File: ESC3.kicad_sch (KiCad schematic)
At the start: 35 parts, among them J10 MOTOR_A, J11 MOTOR_B, J12 MOTOR_C, Q14 Q_NMOS_GDS, Q15 Q_NMOS_GDS, Q16 Q_NMOS_GDS, Q17 Q_NMOS_GDS, Q18 Q_NMOS_GDS, Q19 Q_NMOS_GDS, U18 STM32G071GBUxN, U19 DRV8300D

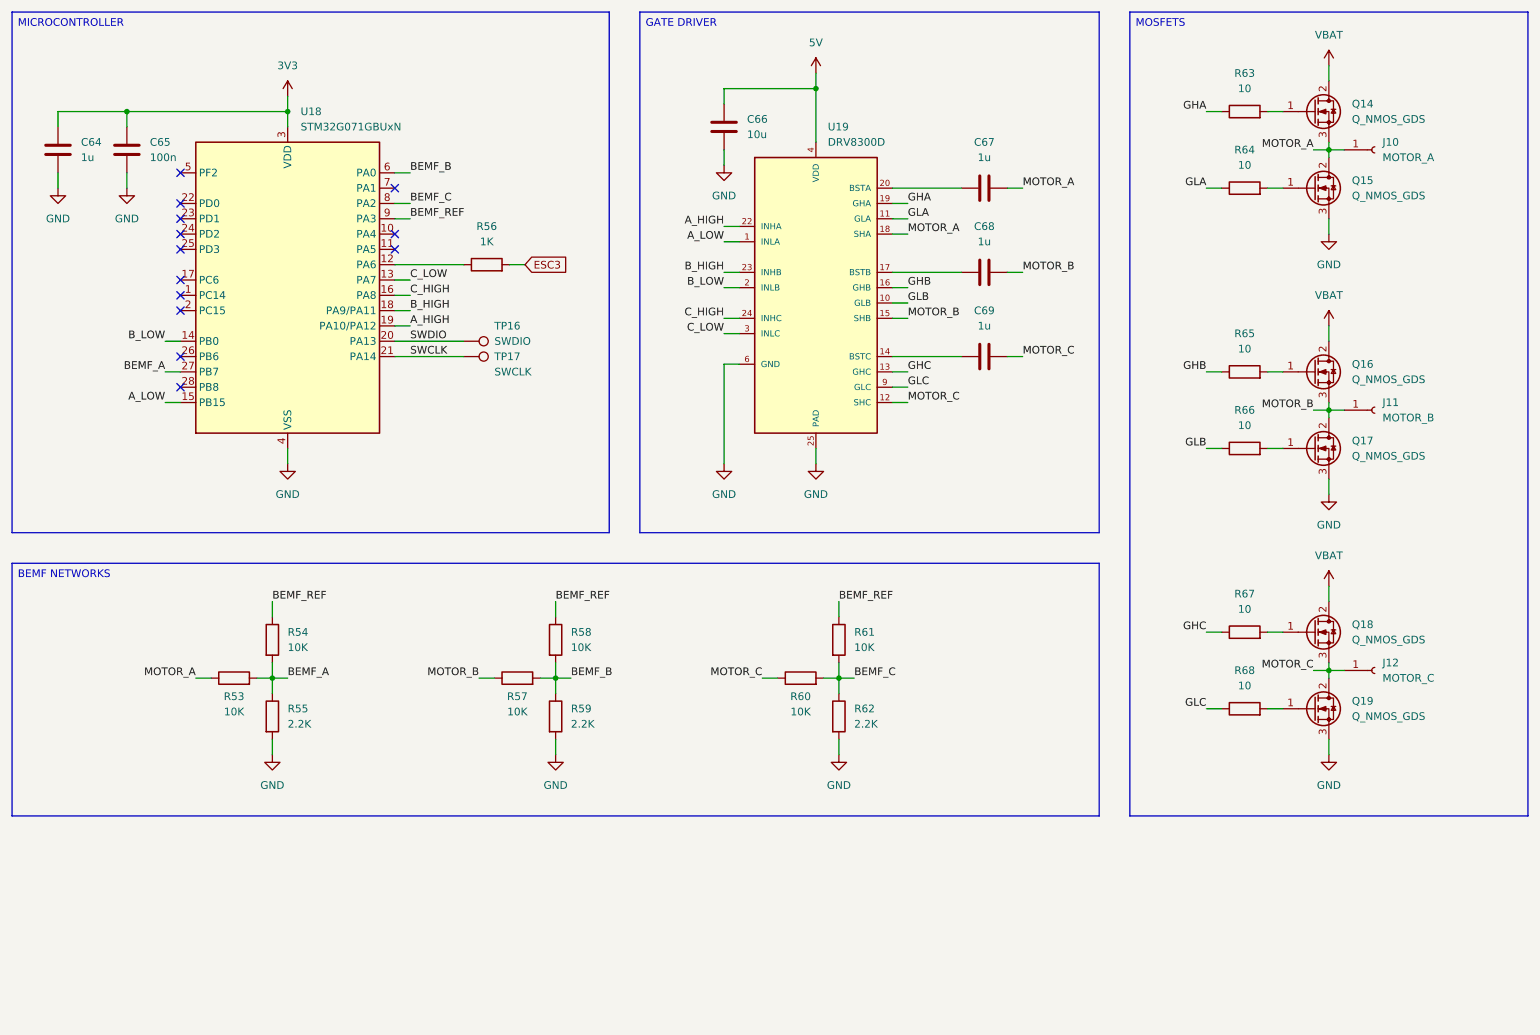
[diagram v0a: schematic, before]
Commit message: Footprints and revision
Added the missing footprints.
Updated a all the schematics.
Completed an initial review of the schematics.

TODO:
Perform a deep review of the schematics before committing to layout.
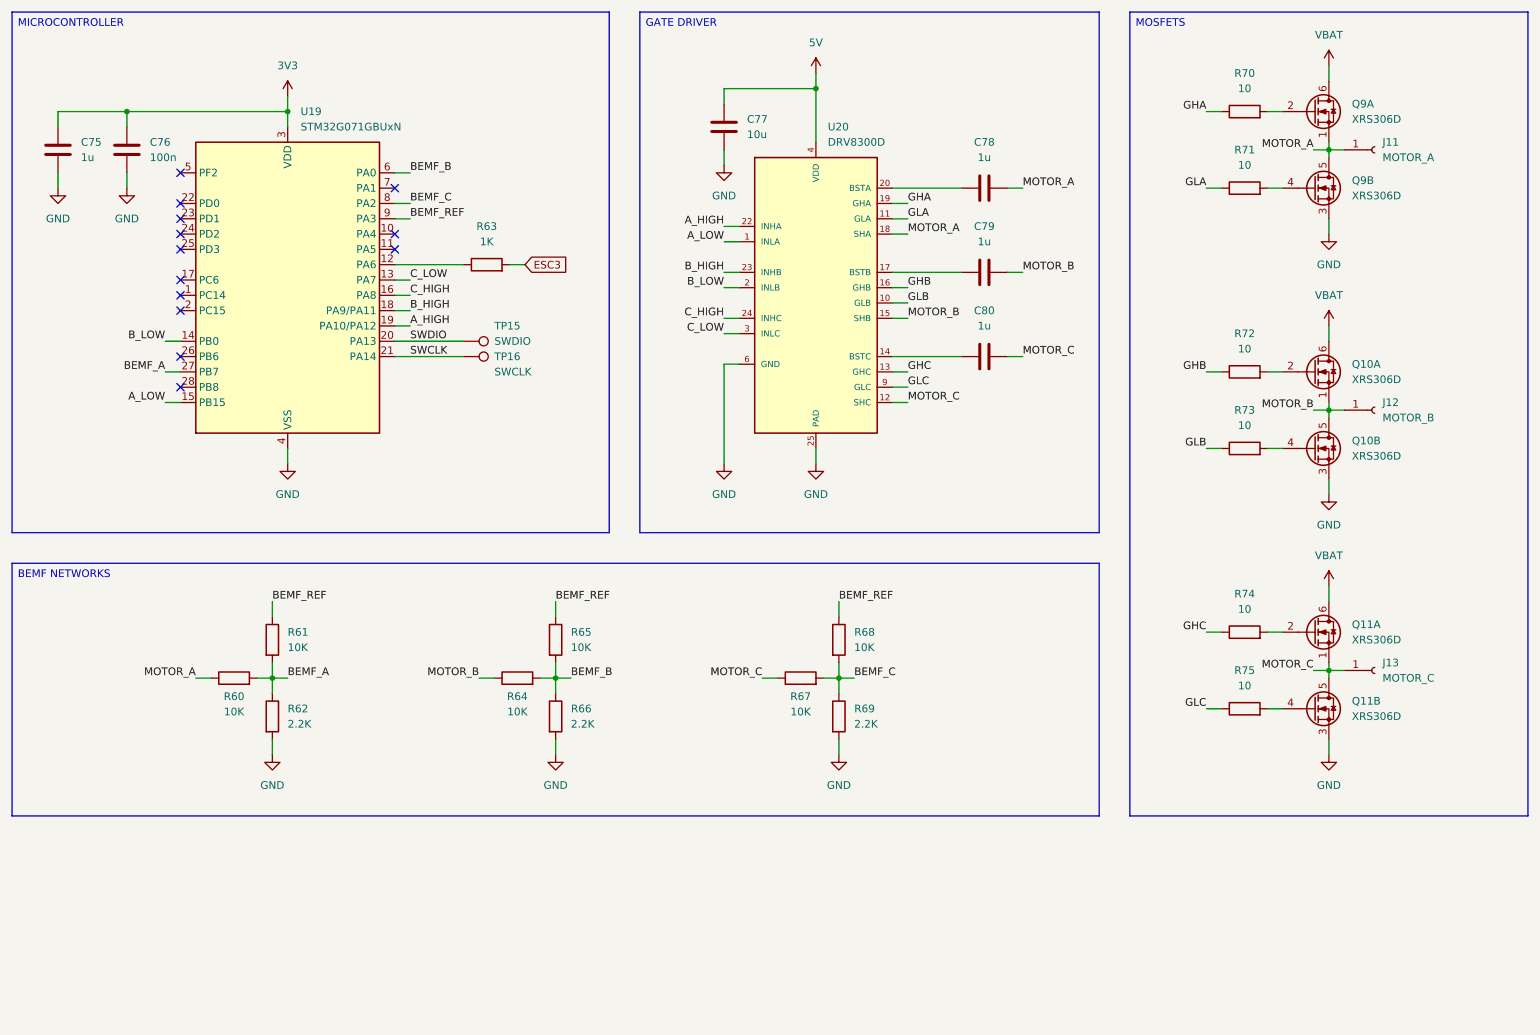
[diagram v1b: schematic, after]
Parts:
- removed Q14, Q15, Q16, Q17, Q18, Q19: Q_NMOS_GDS, symbol Transistor_FET:Q_NMOS_GDS
- added Q10, Q11, Q9: XRS306D, Custom_Parts:PDFN8, symbol Transistor_FET:Q_Dual_NMOS_S1G1S2G2D2D1
- C75: renamed from C64; footprint (none) -> Capacitor_SMD:C_0603_1608Metric
- C76: renamed from C65; footprint (none) -> Capacitor_SMD:C_0603_1608Metric
- C77: renamed from C66; footprint (none) -> Capacitor_SMD:C_0805_2012Metric
- C78: renamed from C67; footprint (none) -> Capacitor_SMD:C_0603_1608Metric
- C79: renamed from C68; footprint (none) -> Capacitor_SMD:C_0603_1608Metric
- C80: renamed from C69; footprint (none) -> Capacitor_SMD:C_0603_1608Metric
- R60: renamed from R53; footprint (none) -> Resistor_SMD:R_0603_1608Metric
- R61: renamed from R54; footprint (none) -> Resistor_SMD:R_0603_1608Metric
- R62: renamed from R55; footprint (none) -> Resistor_SMD:R_0603_1608Metric
- R63: renamed from R56; footprint (none) -> Resistor_SMD:R_0603_1608Metric
- R64: renamed from R57; footprint (none) -> Resistor_SMD:R_0603_1608Metric
- R65: renamed from R58; footprint (none) -> Resistor_SMD:R_0603_1608Metric
- R66: renamed from R59; footprint (none) -> Resistor_SMD:R_0603_1608Metric
- R67: renamed from R60; footprint (none) -> Resistor_SMD:R_0603_1608Metric
- R68: renamed from R61; footprint (none) -> Resistor_SMD:R_0603_1608Metric
- R69: renamed from R62; footprint (none) -> Resistor_SMD:R_0603_1608Metric
- R70: renamed from R63; footprint (none) -> Resistor_SMD:R_0603_1608Metric
- R71: renamed from R64; footprint (none) -> Resistor_SMD:R_0603_1608Metric
- R72: renamed from R65; footprint (none) -> Resistor_SMD:R_0603_1608Metric
- R73: renamed from R66; footprint (none) -> Resistor_SMD:R_0603_1608Metric
- R74: renamed from R67; footprint (none) -> Resistor_SMD:R_0603_1608Metric
- R75: renamed from R68; footprint (none) -> Resistor_SMD:R_0603_1608Metric
- renumbered J10 to J11, J11 to J12, J12 to J13, TP16 to TP15, TP17 to TP16, U18 to U19, U19 to U20
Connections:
- net GND: now also Q10.3 (S), Q11.3 (S), Q9.3 (S)
- net MOTOR_A: now also Q9.1 (S), Q9.5 (D)
- net MOTOR_B: now also Q10.1 (S), Q10.5 (D)
- net MOTOR_C: now also Q11.1 (S), Q11.5 (D)
- net VBAT: now also Q10.6 (D), Q11.6 (D), Q9.6 (D)
- net at R71.2: now also Q9.4 (G)
- net at R70.2: now also Q9.2 (G)
- net at R72.2: now also Q10.2 (G)
- net at R74.2: now also Q11.2 (G)
- net at R73.2: now also Q10.4 (G)
- net at R75.2: now also Q11.4 (G)

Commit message: ESC design
Updated the ESC schematics.
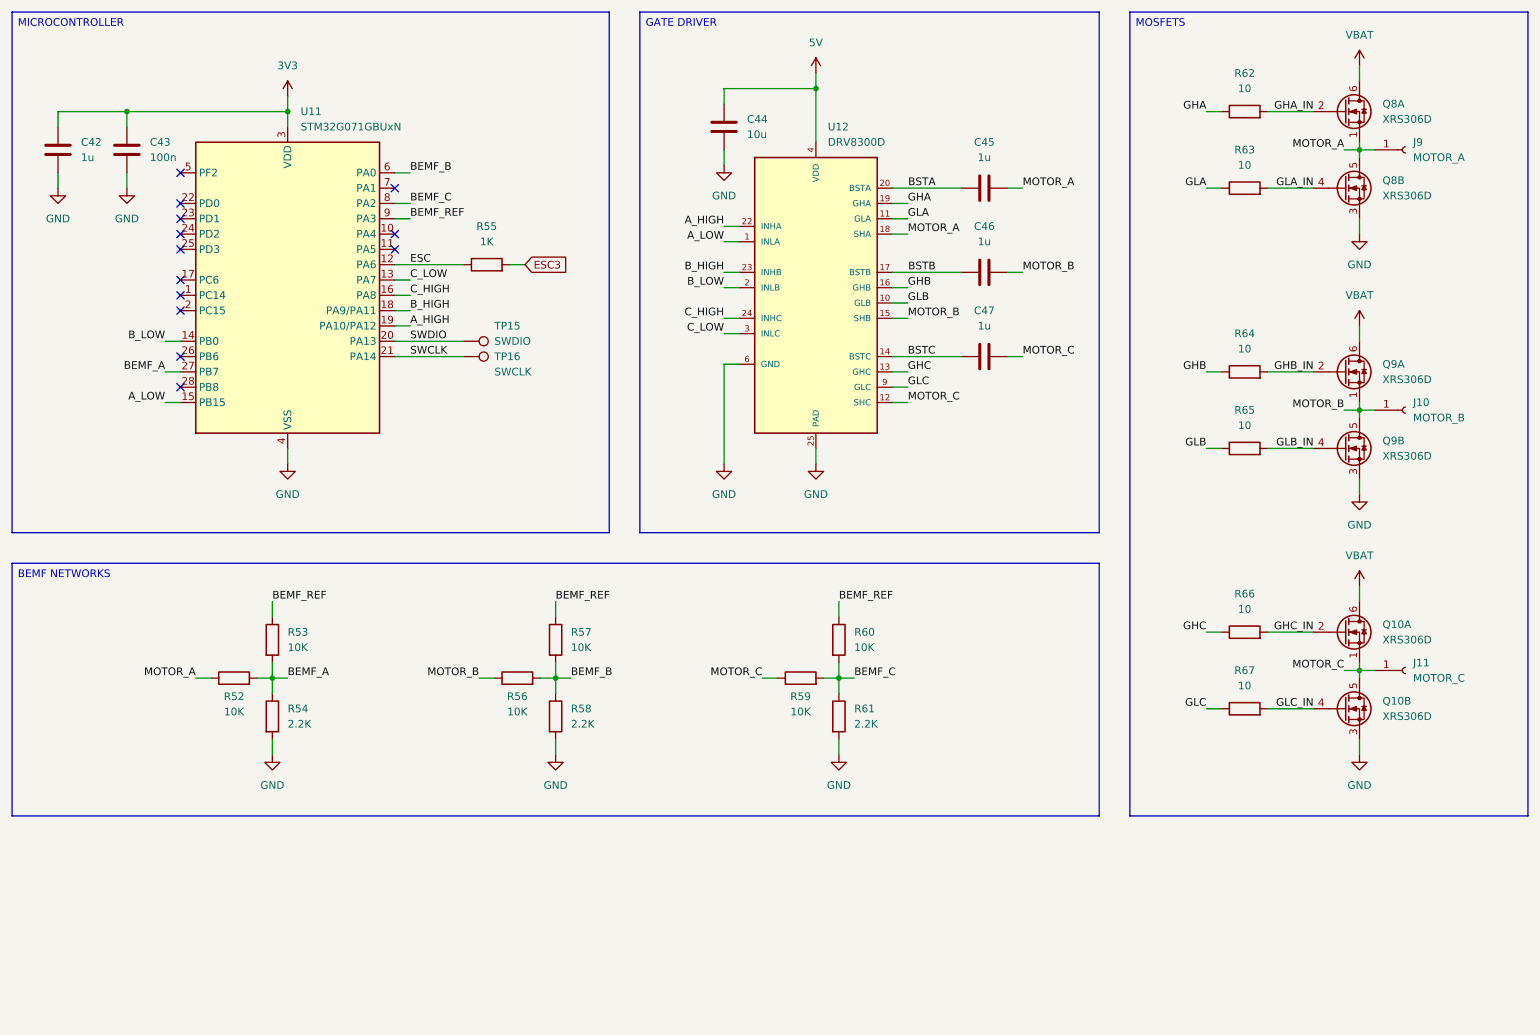
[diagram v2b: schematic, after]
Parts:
- renumbered C75 to C42, C76 to C43, C77 to C44, C78 to C45, C79 to C46, C80 to C47, J12 to J10, J13 to J11, J11 to J9, Q11 to Q10, Q9 to Q8, Q10 to Q9, R60 to R52, R61 to R53, R62 to R54, R63 to R55, R64 to R56, R65 to R57, R66 to R58, R67 to R59, R68 to R60, R69 to R61, R70 to R62, R71 to R63, R72 to R64, R73 to R65, R74 to R66, R75 to R67, U19 to U11, U20 to U12
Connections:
- net BSTC: now reaches C47.1, U12.14 (BSTC)
- net GHA_IN: now reaches Q8.2 (G), R62.2
- net ESC: now reaches R55.1, U11.12 (PA6)
- net GHB_IN: now reaches Q9.2 (G), R64.2
- net GHC_IN: now reaches Q10.2 (G), R66.2
- net BSTA: now reaches C45.1, U12.20 (BSTA)
- net GLA_IN: now reaches Q8.4 (G), R63.2
- net BSTB: now reaches C46.1, U12.17 (BSTB)
- net GLB_IN: now reaches Q9.4 (G), R65.2
- net GLC_IN: now reaches Q10.4 (G), R67.2
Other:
- company: (none) -> DavidMolTor
- title: (none) -> THUNDER HORSE
- moved on the sheet: J10, J11, J9, Q10A, Q10B, Q8A, Q8B, Q9A, Q9B

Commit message: Connectors and tag
Added bulk capacitance for each ESC.
Added SWD connector.
Updated all tags.

TODO:
Add pads for the unconnected GPIO pins.
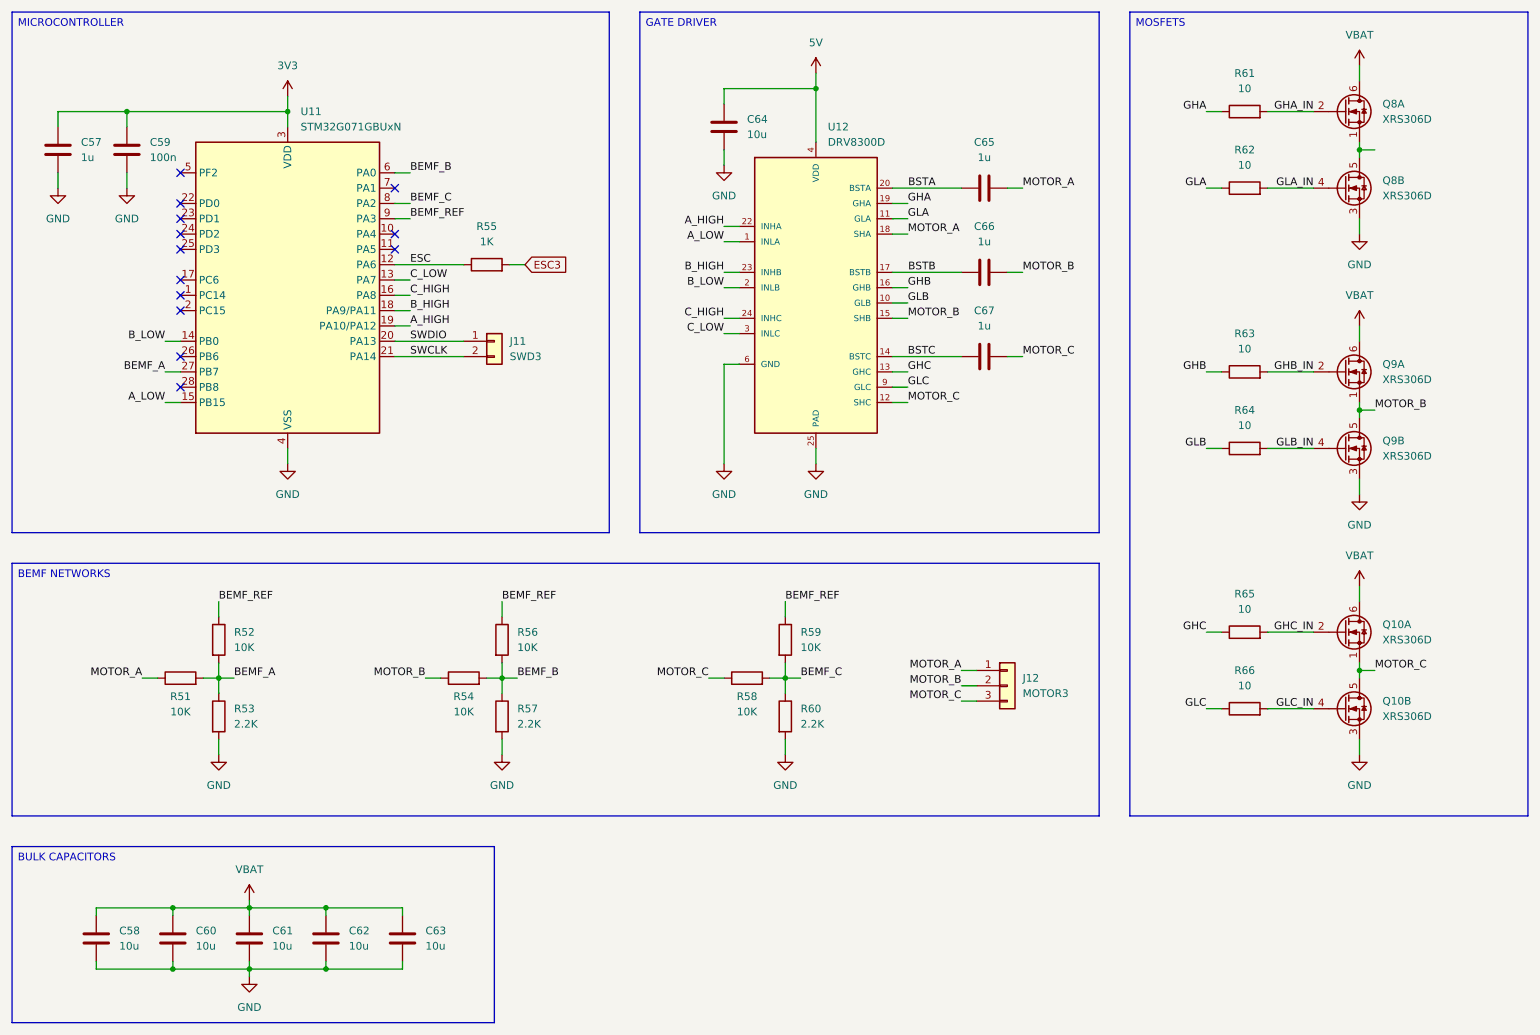
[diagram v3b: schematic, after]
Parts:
- removed J10: MOTOR_B, TestPoint:TestPoint_Pad_D2.0mm, symbol Connector:Conn_01x01_Socket
- removed J11: MOTOR_C, TestPoint:TestPoint_Pad_D2.0mm, symbol Connector:Conn_01x01_Socket
- removed J9: MOTOR_A, TestPoint:TestPoint_Pad_D2.0mm, symbol Connector:Conn_01x01_Socket
- removed R67: 10, Resistor_SMD:R_0603_1608Metric, symbol Device:R
- removed TP15: SWDIO, TestPoint:TestPoint_Pad_D1.0mm, symbol Connector:TestPoint
- removed TP16: SWCLK, TestPoint:TestPoint_Pad_D1.0mm, symbol Connector:TestPoint
- added C58, C60, C61, C62, C63: 10u, symbol Device:C
- added J11: SWD3, symbol Connector_Generic:Conn_01x02
- added J12: MOTOR3, Custom_Parts:PAD_3_SQUARE_SOLID_2.0x2.0mm_P2.5mm, symbol Connector_Generic:Conn_01x03
- added R51: 10K, Resistor_SMD:R_0603_1608Metric, symbol Device:R
- R53, R57, R60: value 10K -> 2.2K
- R54, R58: value 2.2K -> 10K
- R61: value 2.2K -> 10
- renumbered C42 to C57, C43 to C59, C44 to C64, C45 to C65, C46 to C66, C47 to C67
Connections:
- net BEMF_A: now also R53.1, R51.2; no longer R53.2, R54.1
- net BEMF_B: now also R54.2, R57.1; no longer R57.2, R58.1
- net BEMF_C: now also R58.2, R60.1; no longer R60.2, R61.1
- net BEMF_REF: now also R52.1, R56.1, R59.1; no longer R53.1, R57.1, R60.1
- net GHA: now also R61.1; no longer R62.1
- net GHA_IN: now also R61.2; no longer R62.2
- net GHB: now also R63.1; no longer R64.1
- net GHB_IN: now also R63.2; no longer R64.2
- net GHC: now also R65.1; no longer R66.1
- net GHC_IN: now also R65.2; no longer R66.2
- net GLA: now also R62.1; no longer R63.1
- net GLA_IN: now also R62.2; no longer R63.2
- net GLB: now also R64.1; no longer R65.1
- net GLB_IN: now also R64.2; no longer R65.2
- net GLC: now also R66.1
- net GLC_IN: now also R66.2
- net GND: now also R53.2, R57.2, R60.2, C58.2, C60.2, C61.2, C62.2, C63.2; no longer R54.2, R58.2, R61.2
- net MOTOR_A: now also J12.1 (Pin_1), R51.1; no longer Q8.1 (S), Q8.5 (D), R52.1
- net MOTOR_B: now also R54.1, J12.2 (Pin_2); no longer R56.1
- net MOTOR_C: now also R58.1, J12.3 (Pin_3); no longer R59.1
- net SWCLK: now also J11.2 (Pin_2)
- net SWDIO: now also J11.1 (Pin_1)
- net VBAT: now also C58.1, C60.1, C61.1, C62.1, C63.1
- new net: Q8.1 (S), Q8.5 (D)
